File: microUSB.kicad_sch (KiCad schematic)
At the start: 4 parts, among them J11 USB_OTG, U4 TPD4EUSB30

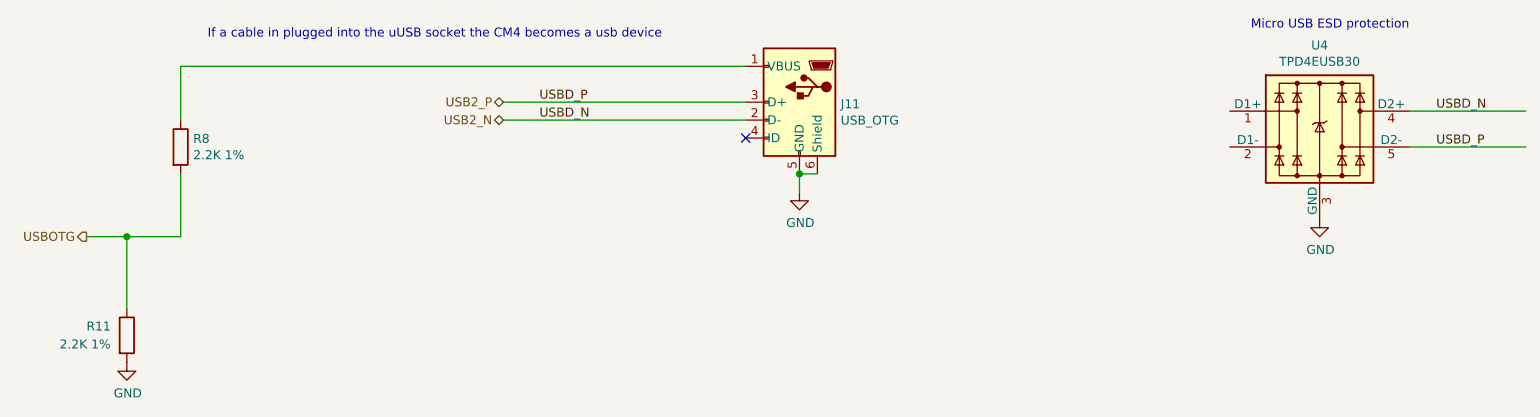
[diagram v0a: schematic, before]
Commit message: Removing unneeded items
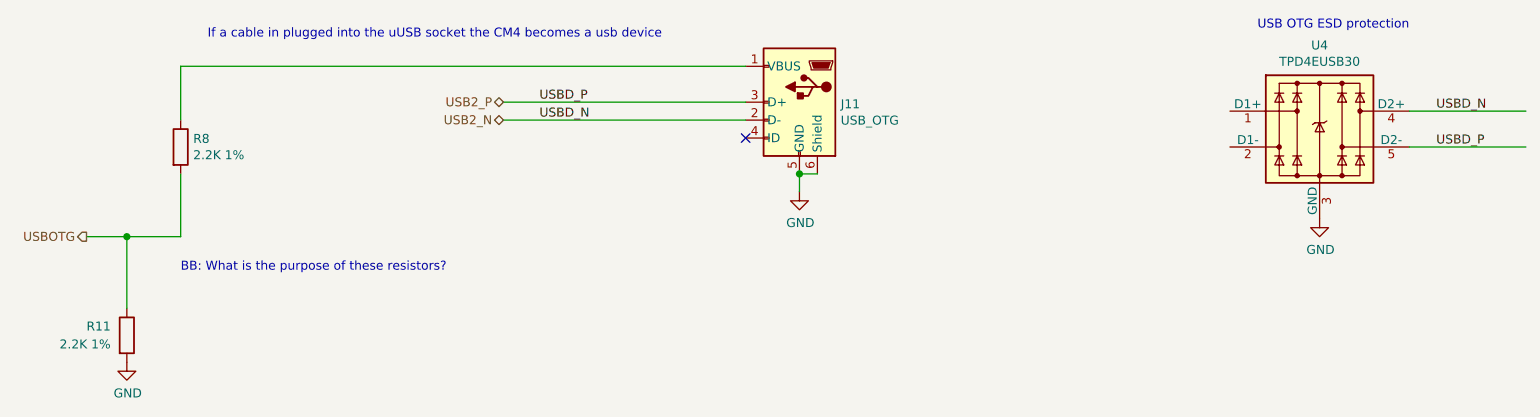
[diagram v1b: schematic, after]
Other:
- note added: "BB: What is the purpose of these resistors?"
- note added: "USB OTG ESD protection"
- note removed: "Micro USB ESD protection"
